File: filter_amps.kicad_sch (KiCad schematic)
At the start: 4 parts, among them U15 LM833DT, U6 LM833DT

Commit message: Schematic is done?
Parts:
- C13, C14: footprint LMK212G_TAY -> Capacitor_SMD:C_0402_1005Metric; symbol CMPE2750:LMK212B7105KGHTR -> CMPE2750:CL05B104KP5NNNC
- U15, U6: value LM833DT -> OPA1678IDR; footprint SO_833DT_STM -> Package_SO:SOIC-8_3.9x4.9mm_P1.27mm
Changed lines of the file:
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@@
 			)
 		)
-		(property "Value" "LM833DT"
+		(property "Value" "OPA1678IDR"
 			(at 120.65 39.37 0)
 			(effects
@@
 			)
 		)
-		(property "Footprint" "SO_833DT_STM"
+		(property "Footprint" "Package_SO:SOIC-8_3.9x4.9mm_P1.27mm"
 			(at 64.77 46.99 0)
 			(effects
@@
 	)
 	(symbol
-		(lib_id "CMPE2750:LMK212B7105KGHTR")
+		(lib_id "CMPE2750:CL05B104KP5NNNC")
 		(at 176.53 39.37 0)
 		(unit 1)
@@
 			)
 		)
-		(property "Footprint" "LMK212G_TAY"
+		(property "Footprint" "Capacitor_SMD:C_0402_1005Metric"
 			(at 176.53 39.37 0)
 			(effects
@@
 			)
 		)
-		(property "Datasheet" "LMK212B7105KGHTR"
+		(property "Datasheet" "CL05B104KP5NNNC"
 			(at 176.53 39.37 0)
 			(effects
@@
 			)
 		)
-		(property "Value" "LM833DT"
+		(property "Value" "OPA1678IDR"
 			(at 120.65 78.74 0)
 			(effects
@@
 			)
 		)
-		(property "Footprint" "SO_833DT_STM"
+		(property "Footprint" "Package_SO:SOIC-8_3.9x4.9mm_P1.27mm"
 			(at 64.77 86.36 0)
 			(effects
@@
 			)
 		)
-		(property "Datasheet" "LM833DT"
+		(property "Datasheet" "OPA1678IDR"
 			(at 64.77 86.36 0)
 			(effects
@@
 	)
 	(symbol
-		(lib_id "CMPE2750:LMK212B7105KGHTR")
+		(lib_id "CMPE2750:CL05B104KP5NNNC")
 		(at 176.53 82.55 0)
 		(unit 1)
@@
 			)
 		)
-		(property "Footprint" "LMK212G_TAY"
+		(property "Footprint" "Capacitor_SMD:C_0402_1005Metric"
 			(at 176.53 82.55 0)
 			(effects
@@
 			)
 		)
-		(property "Datasheet" "LMK212B7105KGHTR"
+		(property "Datasheet" "CL05B104KP5NNNC"
 			(at 176.53 82.55 0)
 			(effects

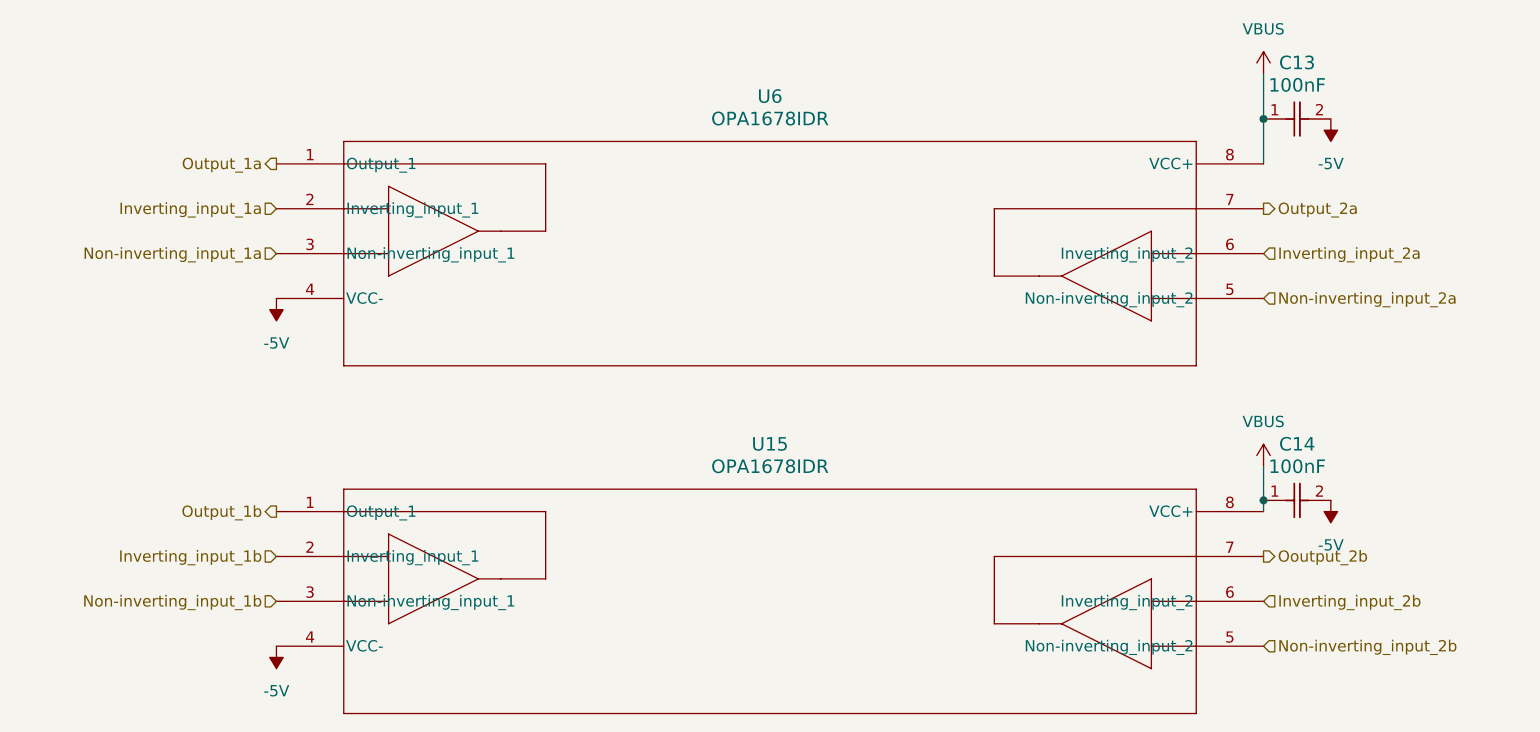
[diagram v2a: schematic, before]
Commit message: Added mounting holes to the schematic, reset the annotations, updated a few footprints, and fixed some issues that were discovered on the ERC.
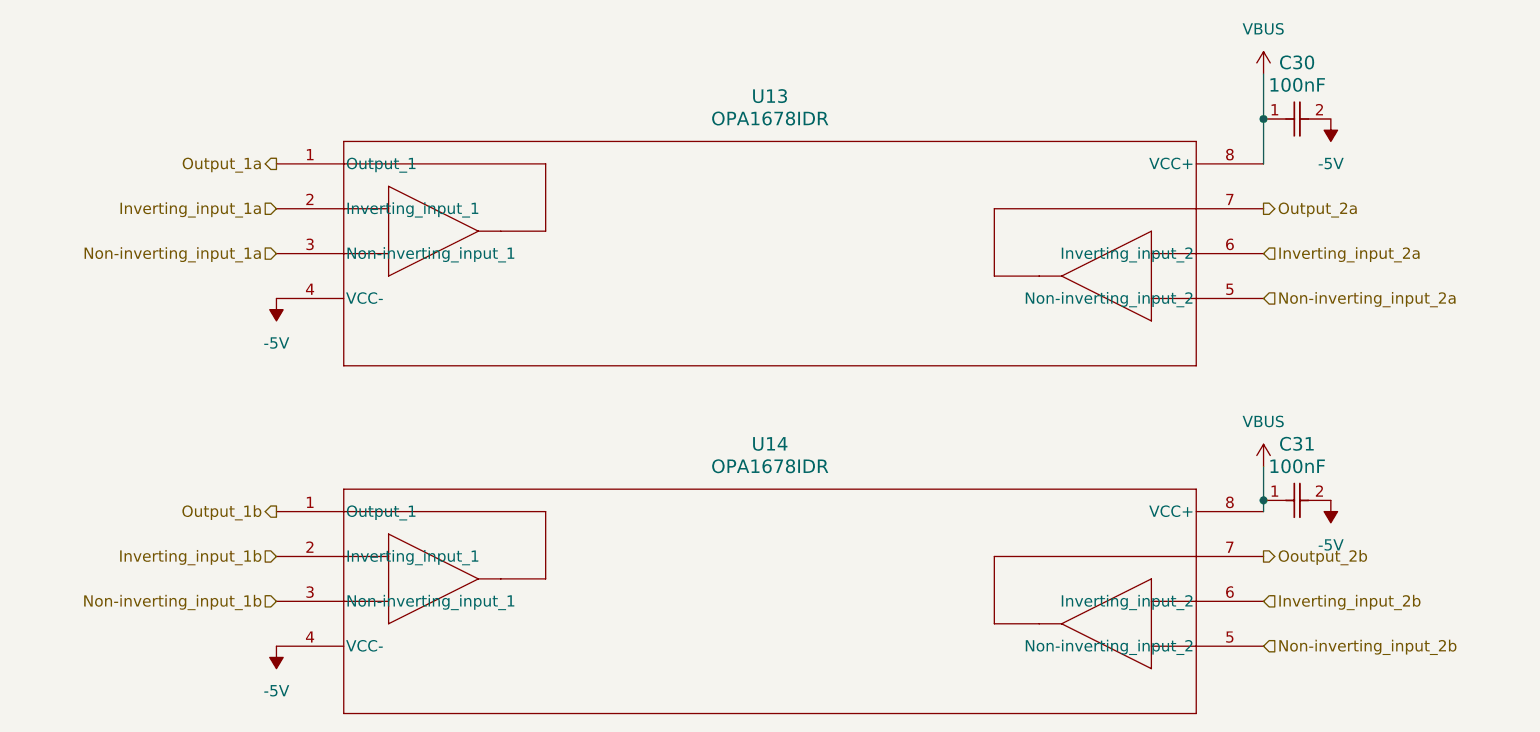
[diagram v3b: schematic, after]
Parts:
- renumbered C13 to C30, C14 to C31, U6 to U13, U15 to U14
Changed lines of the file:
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@@
 		(dnp no)
 		(fields_autoplaced yes)
-		(property "Reference" "U6"
+		(property "Reference" "U13"
 			(at 120.65 36.83 0)
 			(effects
@@
 			(project ""
 				(path "/a86318a1-888d-4137-89a5-221e5a1bc171/d68b35fd-c62c-4cb2-9479-1cd357042dd9/7a5ec571-5e0f-4187-9cd5-35ef9a160b9e"
-					(reference "U6")
+					(reference "U13")
 					(unit 1)
 				)
@@
 		(dnp no)
 		(fields_autoplaced yes)
-		(property "Reference" "C13"
+		(property "Reference" "C30"
 			(at 180.34 33.02 0)
 			(effects
@@
 			(project ""
 				(path "/a86318a1-888d-4137-89a5-221e5a1bc171/d68b35fd-c62c-4cb2-9479-1cd357042dd9/7a5ec571-5e0f-4187-9cd5-35ef9a160b9e"
-					(reference "C13")
+					(reference "C30")
 					(unit 1)
 				)
@@
 		(dnp no)
 		(fields_autoplaced yes)
-		(property "Reference" "#PWR019"
+		(property "Reference" "#PWR0150"
 			(at 176.53 82.55 0)
 			(effects
@@
 			(project ""
 				(path "/a86318a1-888d-4137-89a5-221e5a1bc171/d68b35fd-c62c-4cb2-9479-1cd357042dd9/7a5ec571-5e0f-4187-9cd5-35ef9a160b9e"
-					(reference "#PWR019")
+					(reference "#PWR0150")
 					(unit 1)
 				)
@@
 		(dnp no)
 		(fields_autoplaced yes)
-		(property "Reference" "#PWR0119"
+		(property "Reference" "#PWR0151"
 			(at 184.15 78.74 0)
 			(effects
@@
 			(project "CMPE2750"
 				(path "/a86318a1-888d-4137-89a5-221e5a1bc171/d68b35fd-c62c-4cb2-9479-1cd357042dd9/7a5ec571-5e0f-4187-9cd5-35ef9a160b9e"
-					(reference "#PWR0119")
+					(reference "#PWR0151")
 					(unit 1)
 				)
@@
 		(dnp no)
 		(fields_autoplaced yes)
-		(property "Reference" "U15"
+		(property "Reference" "U14"
 			(at 120.65 76.2 0)
 			(effects
@@
 			(project "CMPE2750"
 				(path "/a86318a1-888d-4137-89a5-221e5a1bc171/d68b35fd-c62c-4cb2-9479-1cd357042dd9/7a5ec571-5e0f-4187-9cd5-35ef9a160b9e"
-					(reference "U15")
+					(reference "U14")
 					(unit 1)
 				)
@@
 		(dnp no)
 		(fields_autoplaced yes)
-		(property "Reference" "#PWR0118"
+		(property "Reference" "#PWR0152"
 			(at 64.77 95.25 0)
 			(effects
@@
 			(project "CMPE2750"
 				(path "/a86318a1-888d-4137-89a5-221e5a1bc171/d68b35fd-c62c-4cb2-9479-1cd357042dd9/7a5ec571-5e0f-4187-9cd5-35ef9a160b9e"
-					(reference "#PWR0118")
+					(reference "#PWR0152")
 					(unit 1)
 				)
@@
 		(dnp no)
 		(fields_autoplaced yes)
-		(property "Reference" "#PWR011"
+		(property "Reference" "#PWR0149"
 			(at 64.77 55.88 0)
 			(effects
@@
 			(project ""
 				(path "/a86318a1-888d-4137-89a5-221e5a1bc171/d68b35fd-c62c-4cb2-9479-1cd357042dd9/7a5ec571-5e0f-4187-9cd5-35ef9a160b9e"
-					(reference "#PWR011")
+					(reference "#PWR0149")
 					(unit 1)
 				)
@@
 		(dnp no)
 		(fields_autoplaced yes)
-		(property "Reference" "#PWR0120"
+		(property "Reference" "#PWR0148"
 			(at 184.15 35.56 0)
 			(effects
@@
 			(project "CMPE2750"
 				(path "/a86318a1-888d-4137-89a5-221e5a1bc171/d68b35fd-c62c-4cb2-9479-1cd357042dd9/7a5ec571-5e0f-4187-9cd5-35ef9a160b9e"
-					(reference "#PWR0120")
+					(reference "#PWR0148")
 					(unit 1)
 				)
@@
 		(dnp no)
 		(fields_autoplaced yes)
-		(property "Reference" "#PWR018"
+		(property "Reference" "#PWR0147"
 			(at 176.53 38.1 0)
 			(effects
@@
 			(project ""
 				(path "/a86318a1-888d-4137-89a5-221e5a1bc171/d68b35fd-c62c-4cb2-9479-1cd357042dd9/7a5ec571-5e0f-4187-9cd5-35ef9a160b9e"
-					(reference "#PWR018")
+					(reference "#PWR0147")
 					(unit 1)
 				)
@@
 		(dnp no)
 		(fields_autoplaced yes)
-		(property "Reference" "C14"
+		(property "Reference" "C31"
 			(at 180.34 76.2 0)
 			(effects
@@
 			(project ""
 				(path "/a86318a1-888d-4137-89a5-221e5a1bc171/d68b35fd-c62c-4cb2-9479-1cd357042dd9/7a5ec571-5e0f-4187-9cd5-35ef9a160b9e"
-					(reference "C14")
-					(unit 1)
-				)
+					(reference "C31")
+					(unit 1)
+				)

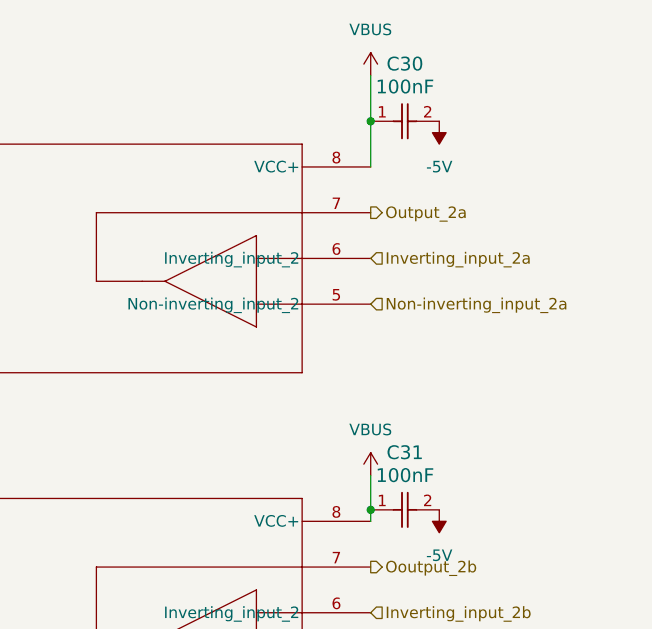
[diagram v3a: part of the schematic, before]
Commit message: Added a ferrite bead and removed a decoupling cap from another ferrite bead
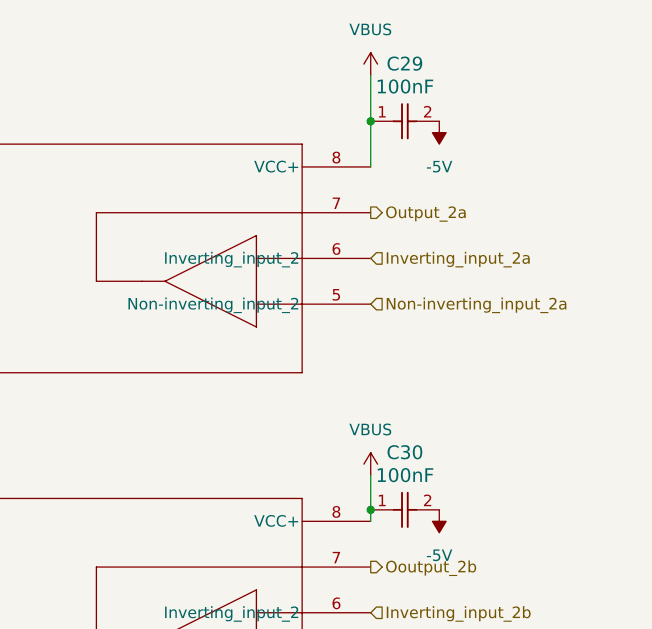
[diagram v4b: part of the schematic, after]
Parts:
- renumbered C30 to C29, C31 to C30
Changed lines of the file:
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@@
 		(dnp no)
 		(fields_autoplaced yes)
-		(property "Reference" "C30"
+		(property "Reference" "C29"
 			(at 180.34 33.02 0)
 			(effects
@@
 			(project ""
 				(path "/a86318a1-888d-4137-89a5-221e5a1bc171/d68b35fd-c62c-4cb2-9479-1cd357042dd9/7a5ec571-5e0f-4187-9cd5-35ef9a160b9e"
-					(reference "C30")
+					(reference "C29")
 					(unit 1)
 				)
@@
 		(dnp no)
 		(fields_autoplaced yes)
-		(property "Reference" "#PWR0150"
+		(property "Reference" "#PWR0149"
 			(at 176.53 82.55 0)
 			(effects
@@
 			(project ""
 				(path "/a86318a1-888d-4137-89a5-221e5a1bc171/d68b35fd-c62c-4cb2-9479-1cd357042dd9/7a5ec571-5e0f-4187-9cd5-35ef9a160b9e"
-					(reference "#PWR0150")
+					(reference "#PWR0149")
 					(unit 1)
 				)
@@
 		(dnp no)
 		(fields_autoplaced yes)
-		(property "Reference" "#PWR0151"
+		(property "Reference" "#PWR0150"
 			(at 184.15 78.74 0)
 			(effects
@@
 			(project "CMPE2750"
 				(path "/a86318a1-888d-4137-89a5-221e5a1bc171/d68b35fd-c62c-4cb2-9479-1cd357042dd9/7a5ec571-5e0f-4187-9cd5-35ef9a160b9e"
-					(reference "#PWR0151")
+					(reference "#PWR0150")
 					(unit 1)
 				)
@@
 		(dnp no)
 		(fields_autoplaced yes)
-		(property "Reference" "#PWR0152"
+		(property "Reference" "#PWR0151"
 			(at 64.77 95.25 0)
 			(effects
@@
 			(project "CMPE2750"
 				(path "/a86318a1-888d-4137-89a5-221e5a1bc171/d68b35fd-c62c-4cb2-9479-1cd357042dd9/7a5ec571-5e0f-4187-9cd5-35ef9a160b9e"
-					(reference "#PWR0152")
+					(reference "#PWR0151")
 					(unit 1)
 				)
@@
 		(dnp no)
 		(fields_autoplaced yes)
-		(property "Reference" "#PWR0149"
+		(property "Reference" "#PWR0148"
 			(at 64.77 55.88 0)
 			(effects
@@
 			(project ""
 				(path "/a86318a1-888d-4137-89a5-221e5a1bc171/d68b35fd-c62c-4cb2-9479-1cd357042dd9/7a5ec571-5e0f-4187-9cd5-35ef9a160b9e"
-					(reference "#PWR0149")
+					(reference "#PWR0148")
 					(unit 1)
 				)
@@
 		(dnp no)
 		(fields_autoplaced yes)
-		(property "Reference" "#PWR0148"
+		(property "Reference" "#PWR0147"
 			(at 184.15 35.56 0)
 			(effects
@@
 			(project "CMPE2750"
 				(path "/a86318a1-888d-4137-89a5-221e5a1bc171/d68b35fd-c62c-4cb2-9479-1cd357042dd9/7a5ec571-5e0f-4187-9cd5-35ef9a160b9e"
-					(reference "#PWR0148")
+					(reference "#PWR0147")
 					(unit 1)
 				)
@@
 		(dnp no)
 		(fields_autoplaced yes)
-		(property "Reference" "#PWR0147"
+		(property "Reference" "#PWR0146"
 			(at 176.53 38.1 0)
 			(effects
@@
 			(project ""
 				(path "/a86318a1-888d-4137-89a5-221e5a1bc171/d68b35fd-c62c-4cb2-9479-1cd357042dd9/7a5ec571-5e0f-4187-9cd5-35ef9a160b9e"
-					(reference "#PWR0147")
+					(reference "#PWR0146")
 					(unit 1)
 				)
@@
 		(dnp no)
 		(fields_autoplaced yes)
-		(property "Reference" "C31"
+		(property "Reference" "C30"
 			(at 180.34 76.2 0)
 			(effects
@@
 			(project ""
 				(path "/a86318a1-888d-4137-89a5-221e5a1bc171/d68b35fd-c62c-4cb2-9479-1cd357042dd9/7a5ec571-5e0f-4187-9cd5-35ef9a160b9e"
-					(reference "C31")
-					(unit 1)
-				)
+					(reference "C30")
+					(unit 1)
+				)
